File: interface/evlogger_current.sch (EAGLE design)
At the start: 10 parts, among them IC1 LMV358SOIC

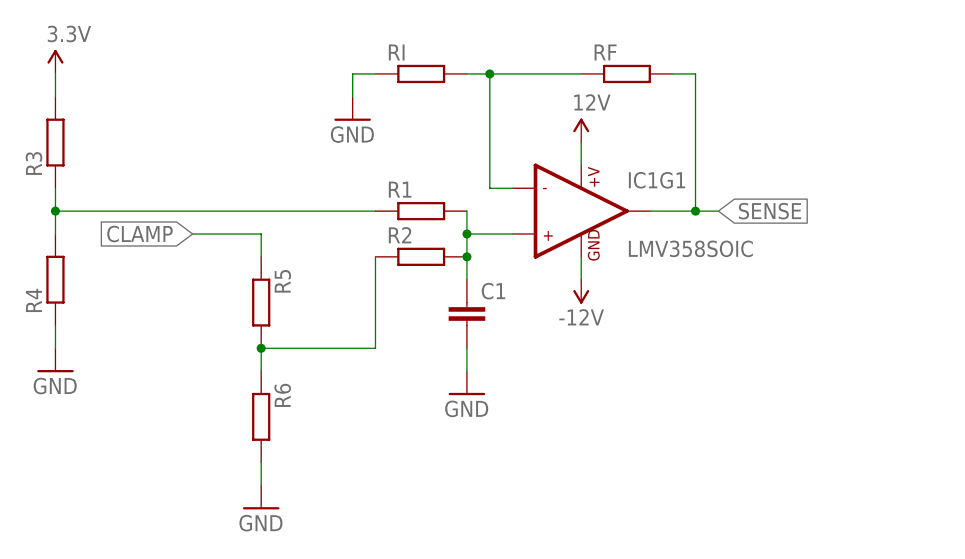
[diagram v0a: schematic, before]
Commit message: Added transient voltage suppression diodes to op amp output
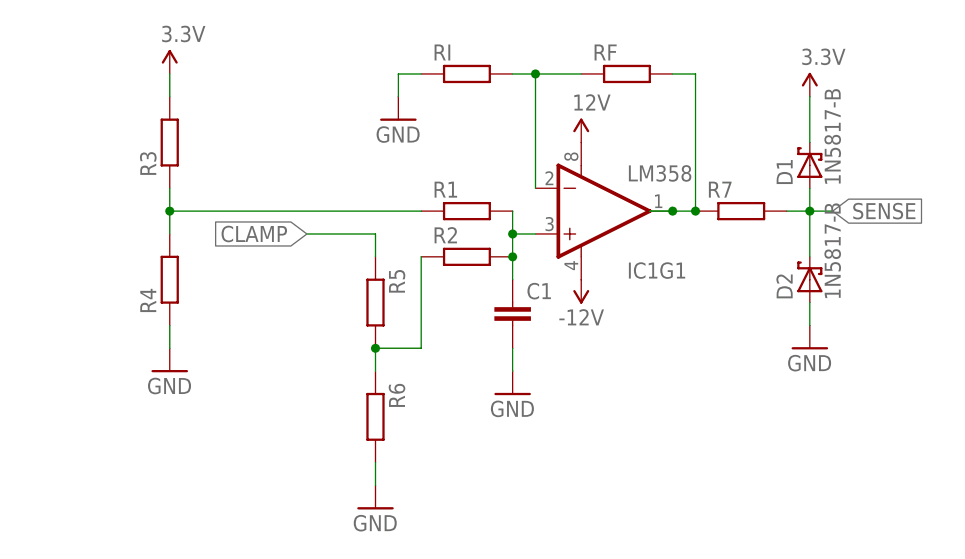
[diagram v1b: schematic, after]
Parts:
- added D1, D2: 1N5817-B, diode:1N5817-B
- added R7: (no value), rcl:R-EU_0207/10
- IC1: value LMV358SOIC -> LM358; device SparkFun-AnalogIC:LMV358SOIC -> SparkFun-AnalogIC:LM358
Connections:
- new net SENS: IC1G1.OUT, R7.1, RF.2
- net 3.3V: now also D1.C
- net GND: now also D2.A
- net N$2: now also IC1G1.-IN; no longer IC1G1.-IN1
- net N$4: now also IC1G1.+IN; no longer IC1G1.+IN1
- net SENSE: now also D1.A, D2.C, R7.2; no longer IC1G1.OUT1, RF.2
- net VCC: now also IC1G1.V+; no longer IC1G1.+V
- net VNEG: now also IC1G1.V-; no longer IC1G1.GND
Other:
- moved on the sheet: C1, R1, R2, R3, R4, R5, R6, RI
